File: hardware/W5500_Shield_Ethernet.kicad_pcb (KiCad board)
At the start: 2 copper layers, 47 x 31 mm, 33 parts, among them J1 HR911105A, J2 Conn_02x05_Odd_Even, U2 W5500, Y1 X322525MOB4SI

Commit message: schematics and photos
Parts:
- moved J2 7.75 mm to (130.6, 64.0), turned to -90 degrees
- moved R1 5.15 mm to (111.5, 62.0), turned to 0 degrees
- moved D1 4.41 mm to (108.0, 61.8), turned to 180 degrees
- moved C10 2.02 mm to (103.9, 62.2)
- moved R2 1.81 mm to (105.0, 62.2)
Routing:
- net RESET_eth: track 14.4 -> 4.27 mm
- net MOSI_eth: track 13.7 -> 6.16 mm
- net SCS_eth: track 8.61 -> 13.8 mm
- net +3.3VA: track 41.3 -> 37.6 mm
- net MISO_eth: track 11.9 -> 8.30 mm
- net SCLK_eth: track 10.1 -> 11.0 mm
- net GND: track 47.8 -> 48.5 mm
- net +3V3: vias 1 -> 0
- added copper zone on F.Cu, net GND
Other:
- board size 47 x 31 mm -> 51.8 x 23.8 mm

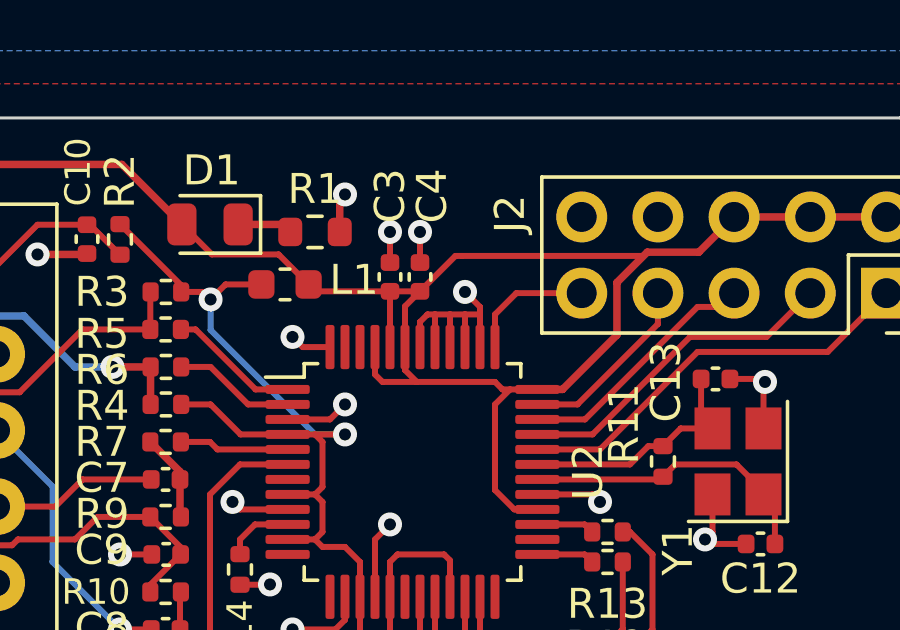
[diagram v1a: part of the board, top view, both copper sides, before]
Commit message: RSVD pins
Estaban conectados a gnd y se dejaron al aire como indica el datasheet
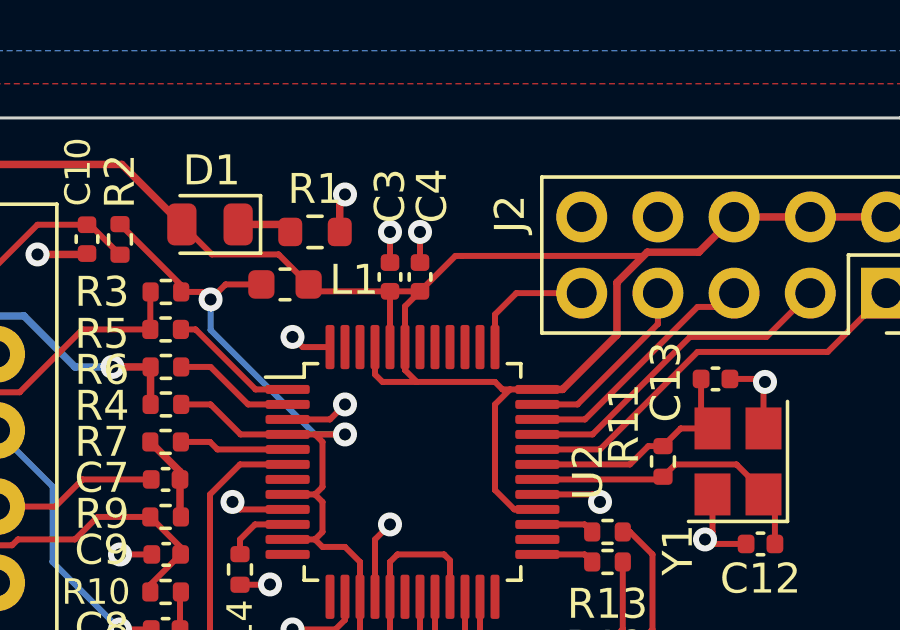
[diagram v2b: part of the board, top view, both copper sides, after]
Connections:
- U2 pad 38: GND -> unconnected-(U2-Pad38)
- U2 pad 39: GND -> unconnected-(U2-Pad39)
- U2 pad 40: GND -> unconnected-(U2-Pad40)
- U2 pad 41: GND -> unconnected-(U2-Pad41)
- U2 pad 42: GND -> unconnected-(U2-Pad42)
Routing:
- net GND: track 48.5 -> 40.2 mm, vias 21 -> 20
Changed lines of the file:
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@@
   (net 39 "unconnected-(U2-Pad46)")
   (net 40 "unconnected-(U2-Pad47)")
+  (net 41 "unconnected-(U2-Pad38)")
+  (net 42 "unconnected-(U2-Pad39)")
+  (net 43 "unconnected-(U2-Pad40)")
+  (net 44 "unconnected-(U2-Pad41)")
+  (net 45 "unconnected-(U2-Pad42)")
   (footprint "Crystal:Crystal_SMD_3225-4Pin_3.2x2.5mm" (layer "F.Cu")
     (at 125.6 69.65 90)
@@
       (net 24 "RESET_eth") (pinfunction "~{RST}") (pintype "input"))
     (pad "38" smd roundrect (at -4.1625 -2.25) (size 0.3 1.475) (layers "F.Cu" "F.Paste" "F.Mask") (roundrect_rratio 0.25)
-      (net 1 "GND") (pinfunction "RSVD") (pintype "input"))
+      (net 41 "unconnected-(U2-Pad38)") (pinfunction "RSVD") (pintype "input+no_connect"))
     (pad "39" smd roundrect (at -4.1625 -1.75) (size 0.3 1.475) (layers "F.Cu" "F.Paste" "F.Mask") (roundrect_rratio 0.25)
-      (net 1 "GND") (pinfunction "RSVD") (pintype "input"))
+      (net 42 "unconnected-(U2-Pad39)") (pinfunction "RSVD") (pintype "input+no_connect"))
     (pad "40" smd roundrect (at -4.1625 -1.25) (size 0.3 1.475) (layers "F.Cu" "F.Paste" "F.Mask") (roundrect_rratio 0.25)
-      (net 1 "GND") (pinfunction "RSVD") (pintype "input"))
+      (net 43 "unconnected-(U2-Pad40)") (pinfunction "RSVD") (pintype "input+no_connect"))
     (pad "41" smd roundrect (at -4.1625 -0.75) (size 0.3 1.475) (layers "F.Cu" "F.Paste" "F.Mask") (roundrect_rratio 0.25)
-      (net 1 "GND") (pinfunction "RSVD") (pintype "input"))
+      (net 44 "unconnected-(U2-Pad41)") (pinfunction "RSVD") (pintype "input+no_connect"))
     (pad "42" smd roundrect (at -4.1625 -0.25) (size 0.3 1.475) (layers "F.Cu" "F.Paste" "F.Mask") (roundrect_rratio 0.25)
-      (net 1 "GND") (pinfunction "RSVD") (pintype "input"))
+      (net 45 "unconnected-(U2-Pad42)") (pinfunction "RSVD") (pintype "input+no_connect"))
     (pad "43" smd roundrect (at -4.1625 0.25) (size 0.3 1.475) (layers "F.Cu" "F.Paste" "F.Mask") (roundrect_rratio 0.25)
       (net 2 "+3V3") (pinfunction "PMODE2") (pintype "input"))
@@
   (segment (start 109.99 73.76) (end 110 73.75) (width 0.2) (layer "F.Cu") (net 1))
   (segment (start 109 73.76) (end 109.99 73.76) (width 0.2) (layer "F.Cu") (net 1))
-  (segment (start 116 64.75) (end 116.5 64.75) (width 0.2) (layer "F.Cu") (net 1))
   (segment (start 124.75 70.75) (end 124.75 72) (width 0.2) (layer "F.Cu") (net 1))
   (segment (start 114.77 77.23) (end 115.5 77.23) (width 0.2) (layer "F.Cu") (net 1))
@@
   (segment (start 107.725 78.275) (end 108.75 77.25) (width 0.2) (layer "F.Cu") (net 1))
   (segment (start 113.5 72.25) (end 114 71.75) (width 0.2) (layer "F.Cu") (net 1))
-  (segment (start 115.5 64.75) (end 116 64.75) (width 0.2) (layer "F.Cu") (net 1))
-  (segment (start 116.5 65.8375) (end 116.5 64.75) (width 0.2) (layer "F.Cu") (net 1))
   (segment (start 115 75.5) (end 114 76.5) (width 0.2) (layer "F.Cu") (net 1))
   (segment (start 117.75 76.25) (end 117 75.5) (width 0.2) (layer "F.Cu") (net 1))
-  (segment (start 115 65) (end 115.25 64.75) (width 0.2) (layer "F.Cu") (net 1))
   (segment (start 126.45 68.55) (end 126.45 67.05) (width 0.2) (layer "F.Cu") (net 1))
   (segment (start 126.4 66.9) (end 126.5 67) (width 0.2) (layer "F.Cu") (net 1))
-  (segment (start 115.25 64.75) (end 115.5 64.75) (width 0.2) (layer "F.Cu") (net 1))
   (segment (start 112 65.8375) (end 111.0875 65.8375) (width 0.2) (layer "F.Cu") (net 1))
   (segment (start 118.9125 70.75) (end 120.75 70.75) (width 0.2) (layer "F.Cu") (net 1))
   (segment (start 117 75.5) (end 117 74.1625) (width 0.2) (layer "F.Cu") (net 1))
-  (segment (start 117 65.8375) (end 117 64.75) (width 0.2) (layer "F.Cu") (net 1))
-  (segment (start 116.5 64) (end 117 64.5) (width 0.2) (layer "F.Cu") (net 1))
   (segment (start 107.725 78.5) (end 107.725 78.275) (width 0.2) (layer "F.Cu") (net 1))
   (segment (start 120.75 70.75) (end 121 71) (width 0.2) (layer "F.Cu") (net 1))
@@
   (segment (start 107.725 78.5) (end 109.25 78.5) (width 0.2) (layer "F.Cu") (net 1))
   (segment (start 112.325 60.925) (end 112.5 60.75) (width 0.25) (layer "F.Cu") (net 1))
-  (segment (start 115 65.8375) (end 115 65) (width 0.2) (layer "F.Cu") (net 1))
   (segment (start 125.87 72.4) (end 124.65 72.4) (width 0.2) (layer "F.Cu") (net 1))
   (segment (start 125.33 66.9) (end 126.4 66.9) (width 0.2) (layer "F.Cu") (net 1))
@@
   (segment (start 115 63.02) (end 115 62) (width 0.2) (layer "F.Cu") (net 1))
   (segment (start 117.75 77.25) (end 117.75 76.25) (width 0.2) (layer "F.Cu") (net 1))
-  (segment (start 116.5 64.75) (end 117 64.75) (width 0.2) (layer "F.Cu") (net 1))
   (segment (start 114 63.02) (end 114 62) (width 0.2) (layer "F.Cu") (net 1))
   (segment (start 112.325 62) (end 112.325 60.925) (width 0.25) (layer "F.Cu") (net 1))
   (segment (start 112.5 74.929651) (end 112.179651 75.25) (width 0.2) (layer "F.Cu") (net 1))
   (segment (start 109 71.25) (end 108.75 71) (width 0.2) (layer "F.Cu") (net 1))
-  (segment (start 117 64.5) (end 117 64.75) (width 0.2) (layer "F.Cu") (net 1))
   (segment (start 126.45 67.05) (end 126.5 67) (width 0.2) (layer "F.Cu") (net 1))
-  (segment (start 115.5 65.8375) (end 115.5 64.75) (width 0.2) (layer "F.Cu") (net 1))
-  (segment (start 116 65.8375) (end 116 64.75) (width 0.2) (layer "F.Cu") (net 1))
   (segment (start 112 68.25) (end 112.5 67.75) (width 0.2) (layer "F.Cu") (net 1))
   (segment (start 106.06 72.75) (end 105 72.75) (width 0.2) (layer "F.Cu") (net 1))
   (via (at 121 71) (size 0.8) (drill 0.4) (layers "F.Cu" "B.Cu") (net 1))
   (via (at 112.5 67.75) (size 0.8) (drill 0.4) (layers "F.Cu" "B.Cu") (net 1))
-  (via (at 116.5 64) (size 0.8) (drill 0.4) (layers "F.Cu" "B.Cu") (net 1))
   (via (at 112.5 60.75) (size 0.8) (drill 0.4) (layers "F.Cu" "B.Cu") (net 1))
   (via (at 109.25 77.25) (size 0.8) (drill 0.4) (layers "F.Cu" "B.Cu") (net 1))
